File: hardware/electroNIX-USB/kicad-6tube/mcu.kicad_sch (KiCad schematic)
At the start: 18 parts, among them Q1 MMBT3904, Q2 MMBT3904, SW1 RESET, SW2 BOOT, SW3 SET, U4 ESP32-WROOM-32E-N4

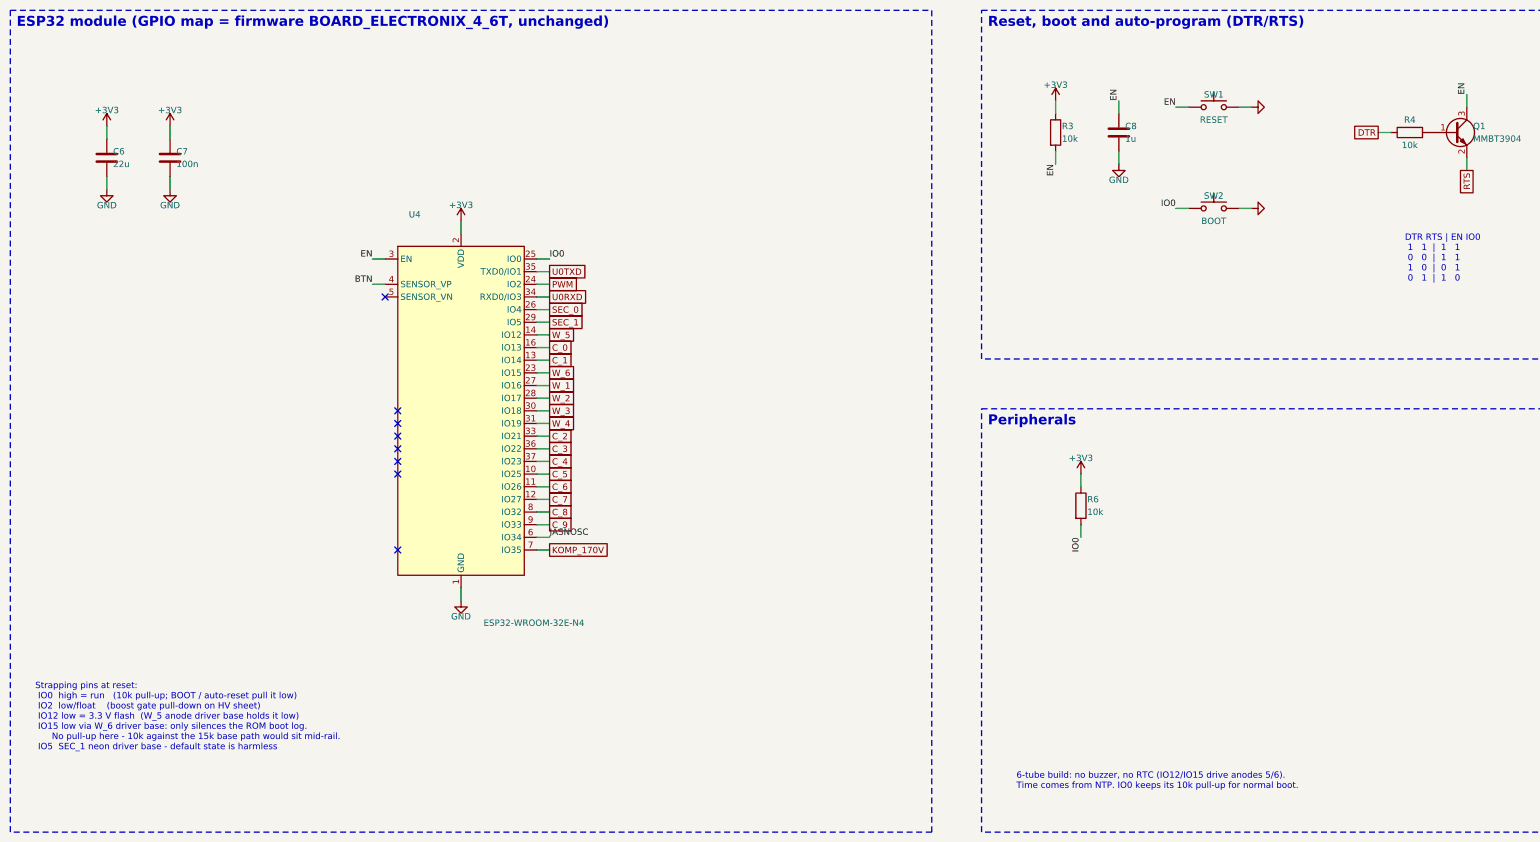
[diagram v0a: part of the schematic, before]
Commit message: electroNIX-USB: drop buzzer and DS3231, run stock firmware
Both builds now match a stock firmware profile with no changes:
BOARD_ELECTRONIX_3 for 4 tubes, BOARD_ELECTRONIX_4_6T for 6 tubes. Time
comes from NTP. IO0 gets a plain 10k pull-up. On the 4-tube build IO12
and IO15 are left open and reserved for anodes 5/6.

Co-Authored-By: Claude Opus 5.5 <noreply@anthropic.com>
Claude-Session: https://claude.ai/code/session_01AFMfevKEKDGbci8uJGhf4W
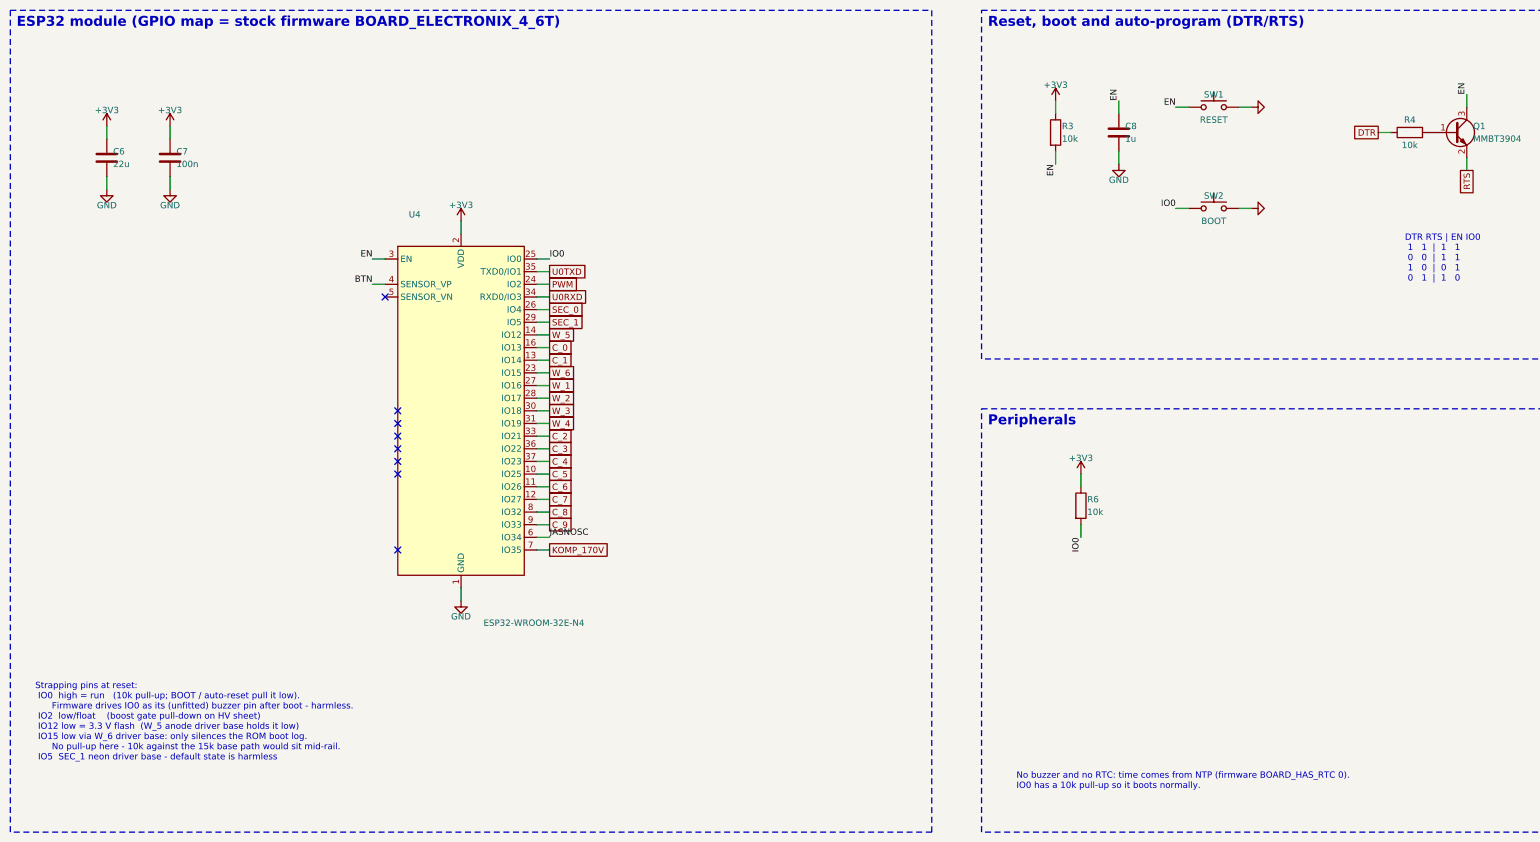
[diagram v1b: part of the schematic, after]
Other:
- note added: "ESP32 module (GPIO map = stock firmware BOARD_ELECTRONIX_4_6T)"
- note added: "No buzzer and no RTC: time comes from NTP (firmware BOARD_HAS_RTC 0). IO0 has a 10k pull-up so it boots normally."
- note added: "Strapping pins at reset: IO0 high = run (10k pull-up; BOOT / auto-reset pull it low). Firmware drives IO0 as its (unfitted) buzzer pin after boot - harmless. IO2 low/float (boost gate pull-down on HV sheet) IO12 low = 3.3 V flash (W_5 anode driver base holds it low) IO15 low via W_6 driver base: only silences the ROM boot log. No pull-up here - 10k against the 15k base path would sit mid-rail. IO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"
- note removed: "6-tube build: no buzzer, no RTC (IO12/IO15 drive anodes 5/6). Time comes from NTP. IO0 keeps its 10k pull-up for normal boot."
- note removed: "ESP32 module (GPIO map = firmware BOARD_ELECTRONIX_4_6T, unchanged)"
- note removed: "Strapping pins at reset: IO0 high = run (10k pull-up; BOOT / auto-reset pull it low) IO2 low/float (boost gate pull-down on HV sheet) IO12 low = 3.3 V flash (W_5 anode driver base holds it low) IO15 low via W_6 driver base: only silences the ROM boot log. No pull-up here - 10k against the 15k base path would sit mid-rail. IO5 SEC_1 neon driver base - default state is harmless"
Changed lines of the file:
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@@
       (type none))
 )
-  (text "ESP32 module (GPIO map = firmware BOARD_ELECTRONIX_4_6T, unchanged)"
+  (text "ESP32 module (GPIO map = stock firmware BOARD_ELECTRONIX_4_6T)"
     (at 21.27 26.27 0)
     (effects
@@
       (justify left top))
 )
-  (text "Strapping pins at reset:\n IO0  high = run   (10k pull-up; BOOT / auto-reset pull it low)\n IO2  low/float    (boost gate pull-down on HV sheet)\n IO12 low = 3.3 V flash  (W_5 anode driver base holds it low)\n IO15 low via W_6 driver base: only silences the ROM boot log.\n      No pull-up here - 10k against the 15k base path would sit mid-rail.\n IO5  SEC_1 neon driver base - default state is harmless"
+  (text "Strapping pins at reset:\n IO0  high = run   (10k pull-up; BOOT / auto-reset pull it low).\n      Firmware drives IO0 as its (unfitted) buzzer pin after boot - harmless.\n IO2  low/float    (boost gate pull-down on HV sheet)\n IO12 low = 3.3 V flash  (W_5 anode driver base holds it low)\n IO15 low via W_6 driver base: only silences the ROM boot log.\n      No pull-up here - 10k against the 15k base path would sit mid-rail.\n IO5  SEC_1 neon driver base - default state is harmless"
     (at 25 160 0)
     (effects
@@
       (justify left top))
 )
-  (text "6-tube build: no buzzer, no RTC (IO12/IO15 drive anodes 5/6).\nTime comes from NTP. IO0 keeps its 10k pull-up for normal boot."
+  (text "No buzzer and no RTC: time comes from NTP (firmware BOARD_HAS_RTC 0).\nIO0 has a 10k pull-up so it boots normally."
     (at 222 178 0)
     (effects

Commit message: electroNIX-USB: socket-adapter footprint, 0.1in neons, 4-tube PCB placement (WIP)
- Z573M socket pins on the electroNIX-2 adapter's 12.6 mm outer ring
  (default footprint), and the direct 9.53 mm footprint resized for the
  1.48 mm socket pins
- Neon_P2.54mm footprint. 6 tubes: HH:MM colon on SEC_0, MM:SS on SEC_1
- SET is a right-angle tact switch; RESET/BOOT use KMR2; low-voltage anode
  resistors moved to 0805
- source/pcb.py: builds the board from the netlist (placement, net
  classes, ESP32 antenna keepout, Freerouting, GND pours, DRC);
  source/fab.sh: fab outputs
- 4-tube board placed (102 x 66 mm, the original kit size), not yet routed

Co-Authored-By: Claude Opus 5.5 <noreply@anthropic.com>
Claude-Session: https://claude.ai/code/session_01AFMfevKEKDGbci8uJGhf4W
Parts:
- SW1, SW2: footprint Button_Switch_SMD:SW_SPST_PTS645 -> Button_Switch_SMD:SW_Push_1P1T_NO_CK_KMR2
- SW3: footprint Button_Switch_THT:SW_PUSH_6mm -> Button_Switch_THT:SW_Tactile_SPST_Angled_PTS645Vx31-2LFS
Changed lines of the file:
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@@
         (font
           (size 1.27 1.27))))
-    (property "Footprint" "Button_Switch_SMD:SW_SPST_PTS645"
+    (property "Footprint" "Button_Switch_SMD:SW_Push_1P1T_NO_CK_KMR2"
       (at 261.62 44.45 0)
       (effects
@@
         (font
           (size 1.27 1.27))))
-    (property "Footprint" "Button_Switch_SMD:SW_SPST_PTS645"
+    (property "Footprint" "Button_Switch_SMD:SW_Push_1P1T_NO_CK_KMR2"
       (at 261.62 64.77 0)
       (effects
@@
           (size 1.27 1.27))
         (justify left)))
-    (property "Footprint" "Button_Switch_THT:SW_PUSH_6mm"
+    (property "Footprint" "Button_Switch_THT:SW_Tactile_SPST_Angled_PTS645Vx31-2LFS"
       (at 384.81 160.02 90)
       (effects

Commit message: electroNIX-USB: drop all switches, regroup board placement by circuit
- No RESET/BOOT/SET: the firmware reads no button, and the CH340C
  DTR/RTS auto-reset handles flashing. SET's pull-up and cap are gone.
- Boost converter is a compact loop (input caps -> L1 -> FET tab) feeding
  the multiplier columns in chain order.
- ESP32: 3V3 decoupling at pin 2, EN RC at pin 3, HV feedback divider and
  clamp at IO35; auto-reset between the CH340C and the module's UART pins.
- Front band spread out: output cap + KBIAS left, cathode row, one anode
  cluster under each tube.
- 6-tube board placed too (150 x 66 mm). Both boards unrouted.

Co-Authored-By: Claude Opus 5.5 <noreply@anthropic.com>
Claude-Session: https://claude.ai/code/session_01AFMfevKEKDGbci8uJGhf4W
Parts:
- removed C10: 100n, Capacitor_SMD:C_0805_2012Metric, symbol Device:C
- removed R8: 10k, Resistor_SMD:R_0805_2012Metric, symbol Device:R
- removed SW1: RESET, Button_Switch_SMD:SW_Push_1P1T_NO_CK_KMR2, symbol Switch:SW_Push
- removed SW2: BOOT, Button_Switch_SMD:SW_Push_1P1T_NO_CK_KMR2, symbol Switch:SW_Push
- removed SW3: SET, Button_Switch_THT:SW_Tactile_SPST_Angled_PTS645Vx31-2LFS, symbol Switch:SW_Push
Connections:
- net BTN: no longer names the net of U4.4 (SENSOR_VP)
- no-connect marks 8 -> 9
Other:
- note added: "No buttons: the CH340C resets the ESP32 and enters download mode through DTR/RTS; unplugging USB is the reset. Recovery if auto-reset ever fails: short the IO0 pull-up (the 10k on IO0) to GND while plugging in."
- note added: "Reset and auto-program (DTR/RTS) - no RESET/BOOT buttons needed"
- note removed: "Reset, boot and auto-program (DTR/RTS)"
